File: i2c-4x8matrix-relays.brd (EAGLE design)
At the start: 130 x 90 mm, 83 parts, among them IC1 MCP23008/SS, IC2 MCP23008/SS, IC3 MCP23008/SS, IC4 MCP23008/SS, IC5 TBD62083AFNG, IC6 TBD62083AFNG, IC7 TBD62083AFNG, IC8 TBD62083AFNG

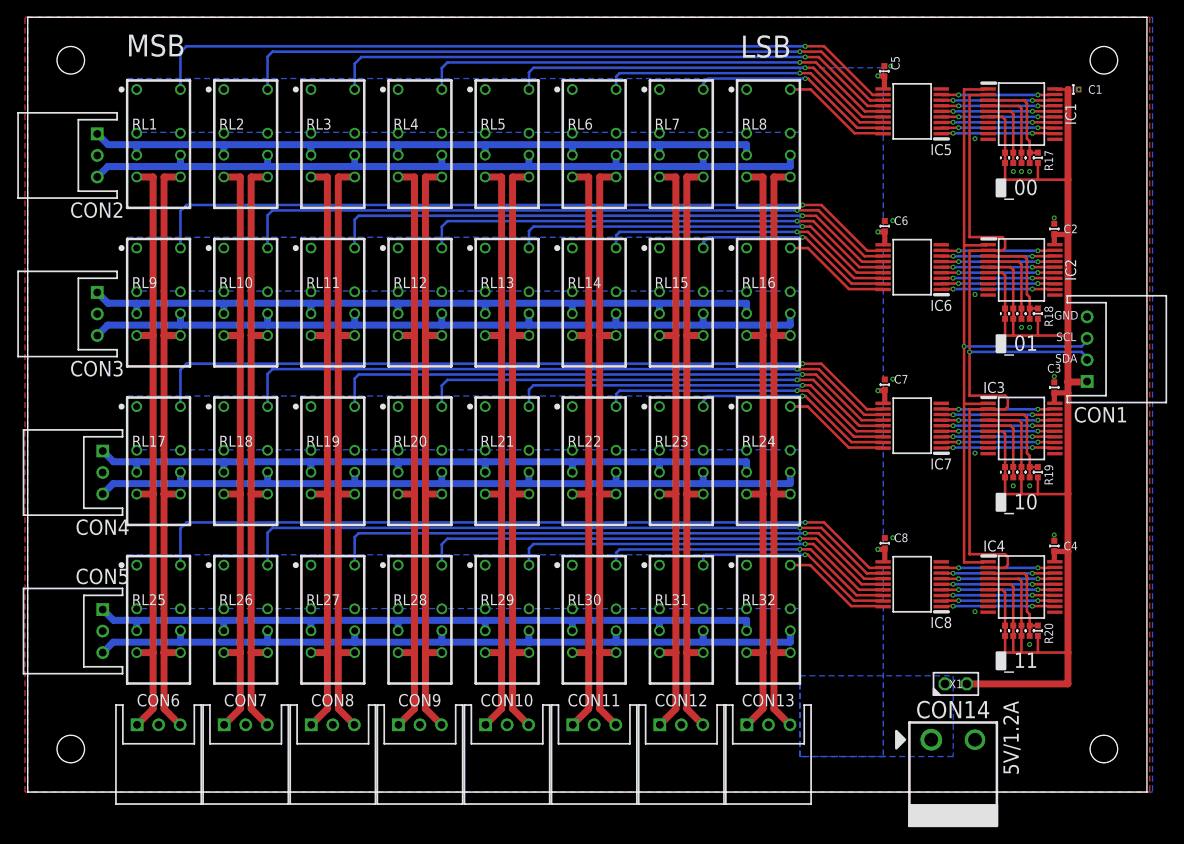
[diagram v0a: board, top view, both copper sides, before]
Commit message: update schematic and layout to use PCA9XXX IO expander
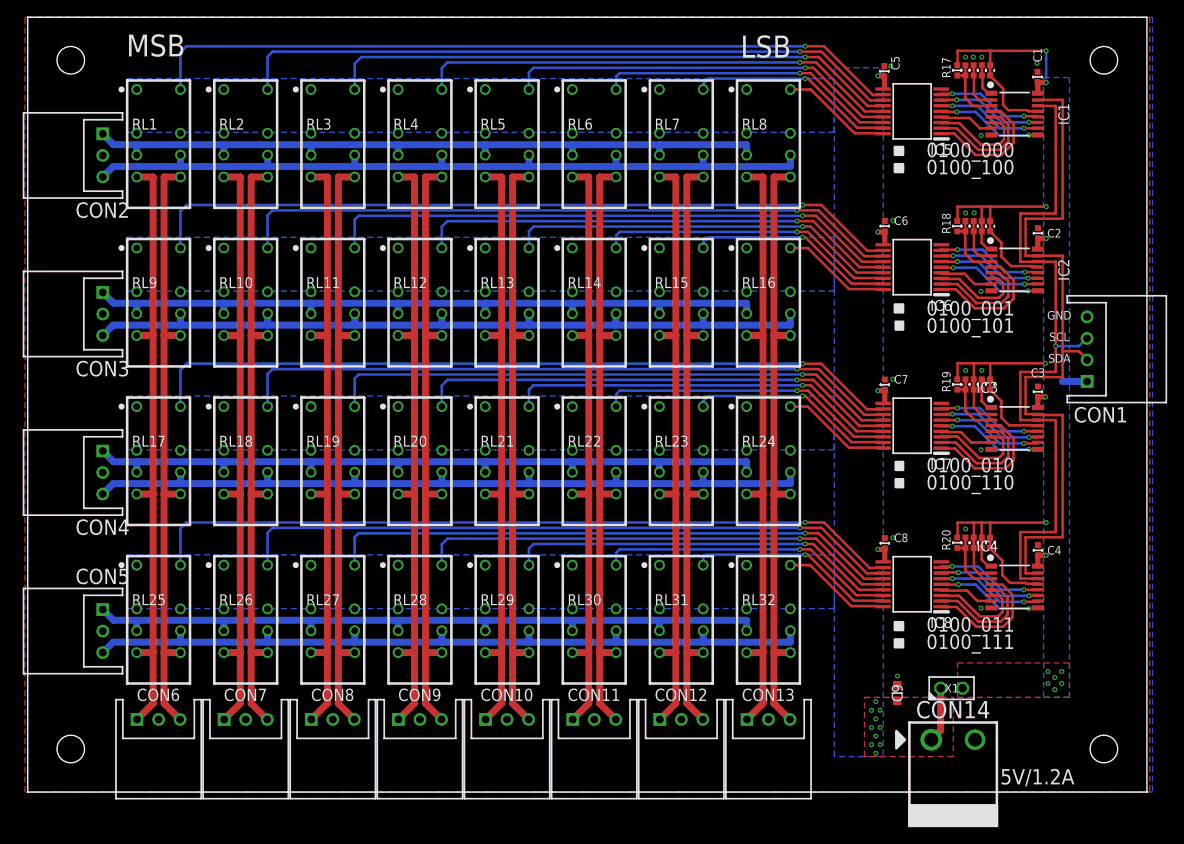
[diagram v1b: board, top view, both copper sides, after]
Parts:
- added C9: (no value), mylib:CR-1608
- IC1, IC2, IC3, IC4: value MCP23008/SS -> PCA9670; device mylib:SOT65P720X530-20N -> mylib:SOT65P510X450X110-16N
- IC5, IC6, IC7, IC8: value TBD62083AFNG -> TBD62183AFNG
- moved R20 13.9 mm to (108.0, 29.0), turned to 270 degrees
- moved R19 13.8 mm to (108.0, 47.3), turned to 270 degrees
- moved R17 13.8 mm to (108.0, 83.8), turned to 270 degrees
- moved R18 13.8 mm to (108.0, 65.7), turned to 270 degrees
- moved R10 12.7 mm to (108.9, 29.0), turned to 270 degrees
- moved R7 12.6 mm to (108.9, 47.3), turned to 270 degrees
- moved R1 12.6 mm to (108.9, 83.8), turned to 270 degrees
- moved R4 12.6 mm to (108.9, 65.7), turned to 270 degrees
- moved R11 11.6 mm to (109.9, 29.0), turned to 270 degrees
- moved R8 11.6 mm to (109.9, 47.3), turned to 270 degrees
- moved R2 11.6 mm to (109.9, 83.8), turned to 270 degrees
- moved R5 11.6 mm to (109.9, 65.7), turned to 270 degrees
- moved R12 10.9 mm to (110.8, 29.0), turned to 270 degrees
- moved R9 10.8 mm to (110.8, 47.3), turned to 270 degrees
- moved R3 10.8 mm to (110.8, 83.8), turned to 270 degrees
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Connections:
- net GND: now also C9.2, IC1.8, IC2.8, IC3.8, IC4.8; no longer IC1.9, IC2.9, IC3.9, IC4.9
- net N$101: now also IC2.1; no longer IC2.5
- net N$102: now also IC2.2; no longer IC2.4
- net N$104: now also IC1.1; no longer IC1.5
- net N$105: now also IC1.2; no longer IC1.4
- net N$107: now also IC1.13; no longer IC1.6
- net N$108: now also IC2.13; no longer IC2.6
- net N$109: now also IC3.13; no longer IC3.6
- net N$110: now also IC4.13; no longer IC4.6
- net N$15: now also IC1.4; no longer IC1.12
- net N$16: now also IC1.5; no longer IC1.13
- net N$26: now also IC1.6; no longer IC1.14
- net N$37: now also IC1.7; no longer IC1.15
- net N$38: now also IC1.9; no longer IC1.16
- net N$53: now also IC1.10; no longer IC1.17
- net N$61: now also IC1.11; no longer IC1.18
- net N$62: now also IC1.12; no longer IC1.19
- net N$63: now also IC2.4; no longer IC2.12
- net N$64: now also IC2.5; no longer IC2.13
- net N$65: now also IC2.6; no longer IC2.14
- net N$66: now also IC2.7; no longer IC2.15
- net N$67: now also IC2.9; no longer IC2.16
- net N$68: now also IC2.10; no longer IC2.17
- net N$69: now also IC2.11; no longer IC2.18
- net N$70: now also IC2.12; no longer IC2.19
- net N$71: now also IC3.4; no longer IC3.12
- net N$72: now also IC3.5; no longer IC3.13
- net N$73: now also IC3.6; no longer IC3.14
- net N$74: now also IC3.7; no longer IC3.15
- net N$75: now also IC3.9; no longer IC3.16
- net N$76: now also IC3.10; no longer IC3.17
- net N$77: now also IC3.11; no longer IC3.18
- net N$78: now also IC3.12; no longer IC3.19
- net N$79: now also IC4.4; no longer IC4.12
- net N$80: now also IC4.5; no longer IC4.13
- net N$81: now also IC4.6; no longer IC4.14
- net N$82: now also IC4.7; no longer IC4.15
- net N$83: now also IC4.9; no longer IC4.16
- net N$84: now also IC4.10; no longer IC4.17
- net N$85: now also IC4.11; no longer IC4.18
- net N$86: now also IC4.12; no longer IC4.19
- net N$89: now also IC1.14, IC2.14, IC3.14, IC4.14; no longer IC1.1, IC2.1, IC3.1, IC4.1
- net N$90: now also IC1.15, IC2.15, IC3.15, IC4.15; no longer IC1.2, IC2.2, IC3.2, IC4.2
- net N$95: now also IC4.1; no longer IC4.5
- net N$96: now also IC4.2; no longer IC4.4
- net N$98: now also IC3.1; no longer IC3.5
- net N$99: now also IC3.2; no longer IC3.4
- net RELAY_POWER: now also C9.1
- net VCC: now also IC1.16, IC2.16, IC3.16, IC4.16; no longer IC1.20, IC2.20, IC3.20, IC4.20
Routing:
- net VCC: track 151.1 -> 82.1 mm, vias 0 -> 14
- net N$90: track 94.7 -> 84.2 mm, vias 1 -> 0
- net N$37: track 13.2 -> 6.38 mm, vias 2 -> 0
- net N$82: track 13.2 -> 6.42 mm, vias 2 -> 0
- net N$74: track 13.2 -> 6.43 mm, vias 2 -> 0
- net N$66: track 13.2 -> 6.45 mm, vias 2 -> 0
- net RELAY_POWER: track 9.75 -> 16.2 mm, vias 4 -> 14
- net N$101: track 7.54 -> 2.77 mm
- net N$98: track 7.54 -> 2.80 mm
- net N$95: track 7.54 -> 2.83 mm
- net N$99: track 9.13 -> 4.44 mm
- net N$104: track 7.54 -> 2.93 mm
- net N$102: track 9.13 -> 4.53 mm
- net N$105: track 9.13 -> 4.53 mm
- net N$100: track 11.5 -> 6.89 mm
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- added copper zone on layer 1, net RELAY_POWER
- added copper zone on layer 1, net VCC
- added copper zone on layer 16, net VCC
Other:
- board text added: "0100_000"
- board text added: "0100_001"
- board text added: "0100_010"
- board text added: "0100_011"
- board text added: "0100_100"
- board text added: "0100_101"
- board text added: "0100_110"
- board text added: "0100_111"
- board text added: "C9"
- board text removed: "_00"
- board text removed: "_01"
- board text removed: "_10"
- board text removed: "_11"
